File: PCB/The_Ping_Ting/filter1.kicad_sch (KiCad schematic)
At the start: 18 parts, among them SW201 SW_SP3T, U104 LM324

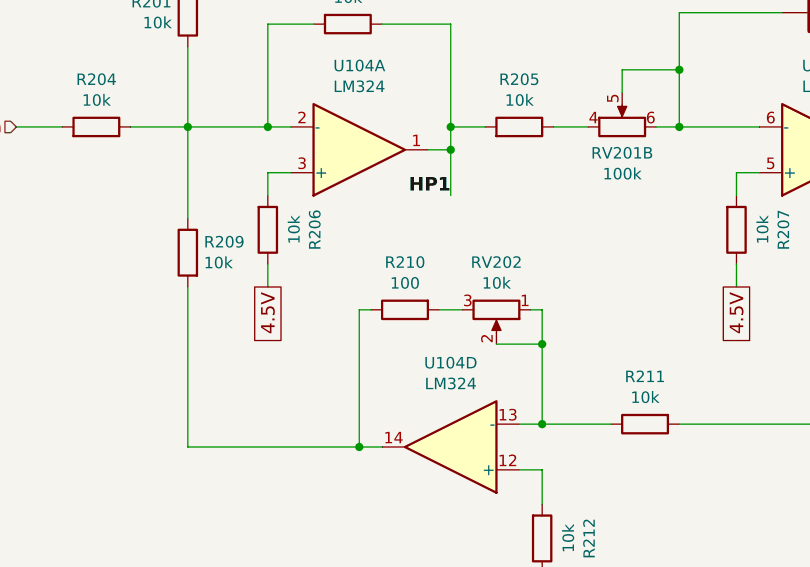
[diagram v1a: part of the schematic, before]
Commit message: REVV 1.2 - Updated resonance feedback resistance Updated the feedback resistance in the mid and high frequency feedback circuit to get a more "stable" resonance level.
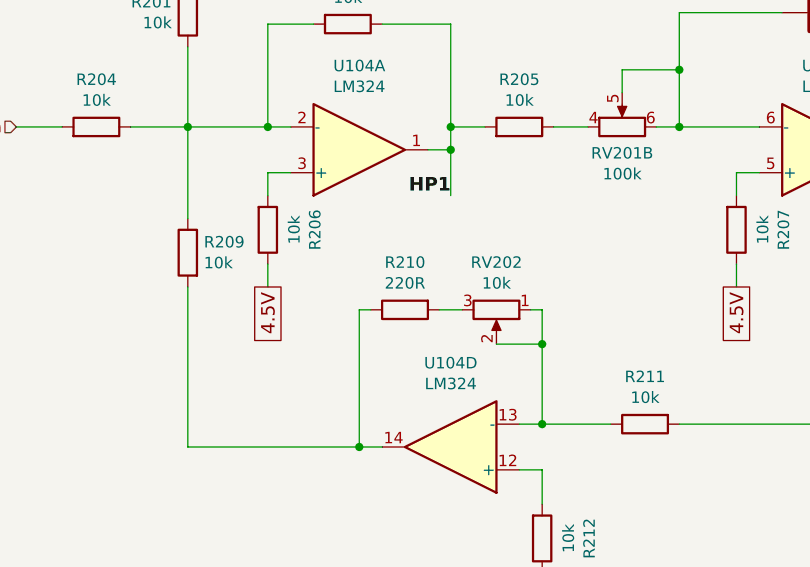
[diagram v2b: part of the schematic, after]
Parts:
- R210: value 100 -> 220R
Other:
- company: (none) -> Kromftronics
- title: (none) -> High Frequency Filter
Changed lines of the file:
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@@
 	(generator_version "8.0")
 	(paper "A4")
+	(title_block
+		(title "High Frequency Filter")
+		(date "2024-09-07")
+		(rev "1.2")
+		(company "Kromftronics")
+	)
 	(junction
 		(at 166.37 91.44)
@@
 			)
 		)
-		(property "Value" "100"
+		(property "Value" "220R"
 			(at 109.22 106.2736 90)
 			(effects
